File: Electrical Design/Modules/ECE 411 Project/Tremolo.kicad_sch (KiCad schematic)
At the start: 14 parts, among them Q1 NPN, U7 TL072

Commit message: kicad business
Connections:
- net In renamed TREMIN
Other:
- company: (none) -> Portland State University
- title: (none) -> Tremolo Effect
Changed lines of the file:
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@@
 	(generator_version "8.0")
 	(paper "A4")
+	(title_block
+		(title "Tremolo Effect")
+		(date "2024-10-31")
+		(rev "1.1")
+		(company "Portland State University")
+		(comment 1 "Open Source Hardware")
+		(comment 2 "Design: Eric Sanman, Sierra Buckley, Chuong Vo, Chris Crider")
+	)
 	(junction
 		(at 100.33 142.24)
@@
 		)
 	)
-	(hierarchical_label "In"
+	(hierarchical_label "TREMIN"
 		(shape input)
 		(at 99.06 80.01 90)
@@
 		)
 	)
-	(hierarchical_label "Out"
+	(hierarchical_label "TREMOUT"
 		(shape output)
 		(at 143.51 80.01 0)

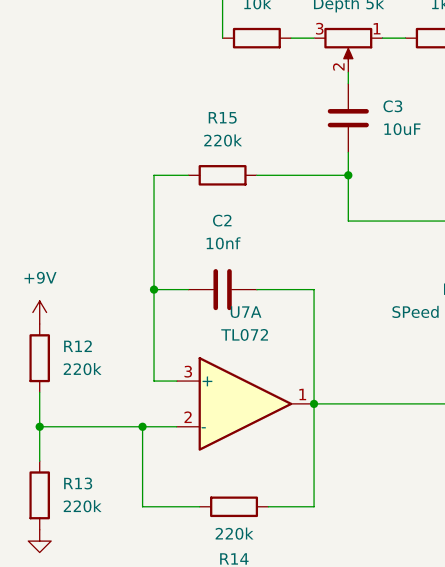
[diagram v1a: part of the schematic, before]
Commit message: add psu and fix schematic
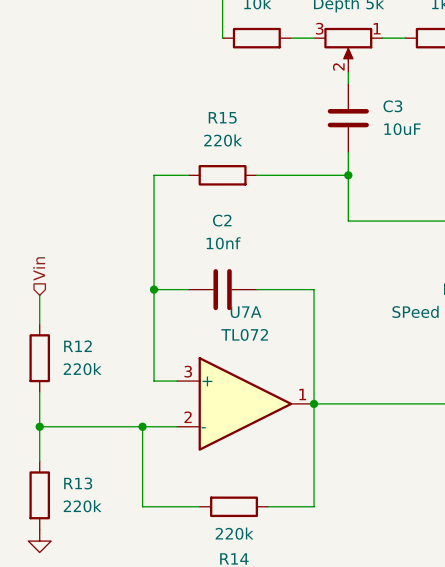
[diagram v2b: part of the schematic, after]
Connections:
- net +9V renamed Vin
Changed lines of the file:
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@@
+	(wire
+		(pts
+			(xy 87.63 142.875) (xy 87.63 146.05)
+		)
+		(stroke
+			(width 0)
+			(type default)
+		)
+	)
 	(wire
 		(pts
@@
 		)
 	)
+	(hierarchical_label "Vin"
+		(shape input)
+		(at 87.63 142.875 90)
+		(fields_autoplaced yes)
+		(effects
+			(font
+				(size 1.27 1.27)
+			)
+			(justify left)
+		)
+	)
 	(hierarchical_label "TREMOUT"
 		(shape output)
@@
 					(unit 1)
 				)
-			)
-		)
-	)
-	(symbol
-		(lib_id "power:+9V")
-		(at 87.63 146.05 0)
-		(unit 1)
-		(exclude_from_sim no)
-		(in_bom yes)
-		(on_board yes)
-		(dnp no)
-		(fields_autoplaced yes)
-		(property "Reference" "#PWR09"
-			(at 87.63 149.86 0)
-			(effects
-				(font
-					(size 1.27 1.27)
-				)
-				(hide yes)
-			)
-		)
-		(property "Value" "+9V"
-			(at 87.63 140.97 0)
-			(effects
-				(font
-					(size 1.27 1.27)
-				)
-			)
-		)
-		(property "Footprint" ""
-			(at 87.63 146.05 0)
-			(effects
-				(font
-					(size 1.27 1.27)
-				)
-				(hide yes)
-			)
-		)
-		(property "Datasheet" ""
-			(at 87.63 146.05 0)
-			(effects
-				(font
-					(size 1.27 1.27)
-				)
-				(hide yes)
-			)
-		)
-		(property "Description" "Power symbol creates a global label with name \"+9V\""
-			(at 87.63 146.05 0)
-			(effects
-				(font
-					(size 1.27 1.27)
-				)
-				(hide yes)
-			)
-		)
-		(pin "1"
-		)
-		(instances
-			(project ""
-				(path "/2625e5a1-d0c8-41ce-941d-75d035a5f1c5/29e94901-2eb6-4d5f-9450-5a88f29fead6"
-					(reference "#PWR09")
-					(unit 1)
-				)

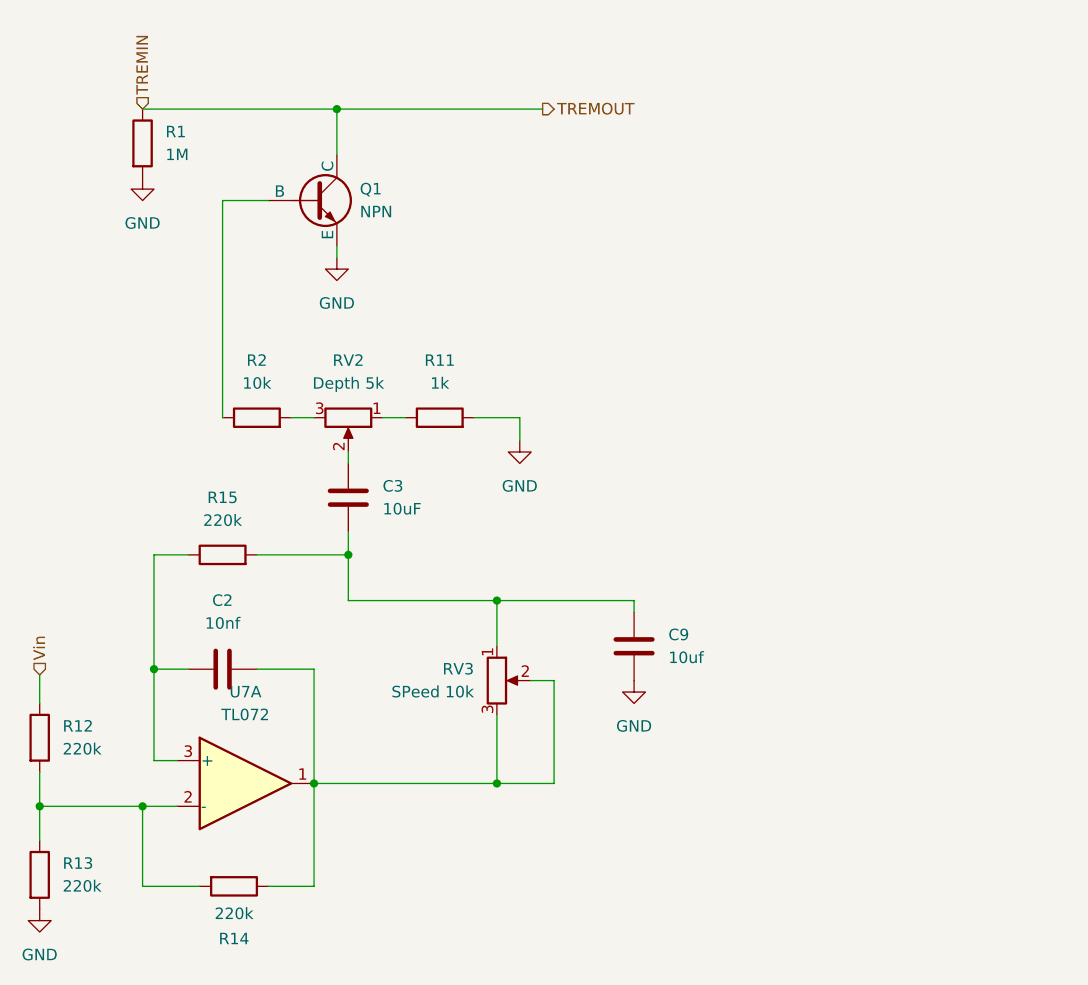
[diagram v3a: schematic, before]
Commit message: schematic, start layout
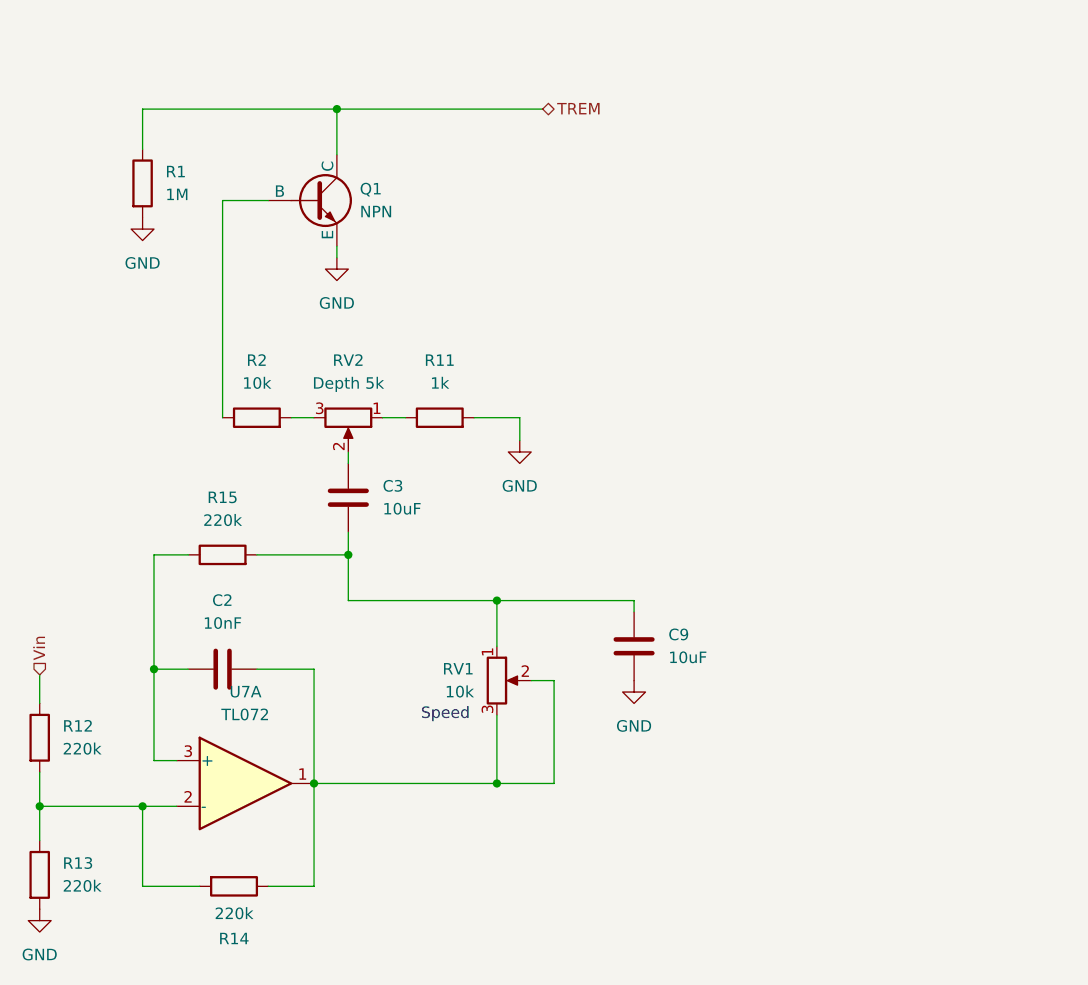
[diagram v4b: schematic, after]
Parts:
- C2: value 10nf -> 10nF; footprint (none) -> Capacitor_SMD:C_0805_2012Metric_Pad1.18x1.45mm_HandSolder
- C3: footprint (none) -> Capacitor_SMD:C_1210_3225Metric_Pad1.33x2.70mm_HandSolder
- C9: value 10uf -> 10uF; footprint (none) -> Capacitor_SMD:C_1206_3216Metric_Pad1.33x1.80mm_HandSolder
- Q1: footprint (none) -> Package_TO_SOT_THT:TO-52-3
- R1, R11, R12, R13, R14, R15, R2: footprint (none) -> Resistor_SMD:R_0805_2012Metric_Pad1.20x1.40mm_HandSolder
- RV1: renamed from RV3; value SPeed 10k -> 10k; footprint (none) -> Connector_PinHeader_2.54mm:PinHeader_1x03_P2.54mm_Vertical
- RV2: footprint (none) -> Connector_PinHeader_2.54mm:PinHeader_1x03_P2.54mm_Vertical
- U7: footprint (none) -> Package_DIP:CERDIP-8_W7.62mm_SideBrazed
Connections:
- net TREMIN renamed TREM
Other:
- note added: "Speed"
- moved on the sheet: R1
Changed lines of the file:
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@@
 	(title_block
 		(title "Tremolo Effect")
-		(date "2024-10-31")
-		(rev "1.1")
+		(date "2024-11-07")
+		(rev "1.5")
 		(company "Portland State University")
 		(comment 1 "Open Source Hardware")
@@
 	(wire
 		(pts
+			(xy 118.11 154.94) (xy 138.43 154.94)
+		)
+		(stroke
+			(width 0)
+			(type default)
+		)
+	)
+	(wire
+		(pts
 			(xy 121.92 119.38) (xy 121.92 118.11)
 		)
@@
 	(wire
 		(pts
+			(xy 99.06 80.01) (xy 99.06 84.455)
+		)
+		(stroke
+			(width 0)
+			(type default)
+		)
+	)
+	(wire
+		(pts
 			(xy 107.95 90.17) (xy 107.95 114.3)
 		)
@@
 		)
 	)
-	(wire
-		(pts
-			(xy 138.43 154.94) (xy 118.11 154.94)
-		)
-		(stroke
-			(width 0)
-			(type default)
-		)
-	)
-	(hierarchical_label "TREMIN"
-		(shape input)
-		(at 99.06 80.01 90)
-		(fields_autoplaced yes)
+	(text "Speed"
+		(exclude_from_sim no)
+		(at 132.715 147.32 0)
 		(effects
 			(font
 				(size 1.27 1.27)
 			)
-			(justify left)
 		)
 	)
@@
 		)
 	)
-	(hierarchical_label "TREMOUT"
-		(shape output)
+	(hierarchical_label "TREM"
+		(shape bidirectional)
 		(at 143.51 80.01 0)
 		(fields_autoplaced yes)
@@
 		(dnp no)
 		(fields_autoplaced yes)
-		(property "Reference" "RV3"
+		(property "Reference" "RV1"
 			(at 135.89 142.2399 0)
 			(effects
@@
 			)
 		)
-		(property "Value" "SPeed 10k"
+		(property "Value" "10k"
 			(at 135.89 144.7799 0)
 			(effects
@@
 			)
 		)
-		(property "Footprint" ""
+		(property "Footprint" "Connector_PinHeader_2.54mm:PinHeader_1x03_P2.54mm_Vertical"
 			(at 138.43 143.51 0)
 			(effects
@@
 			(project "ECE 411 Project"
 				(path "/2625e5a1-d0c8-41ce-941d-75d035a5f1c5/29e94901-2eb6-4d5f-9450-5a88f29fead6"
-					(reference "RV3")
+					(reference "RV1")
 					(unit 1)
 				)
@@
 			)
 		)
-		(property "Footprint" ""
+		(property "Footprint" "Package_TO_SOT_THT:TO-52-3"
 			(at 181.61 90.17 0)
 			(effects
@@
 			)
 		)
-		(property "Footprint" ""
+		(property "Footprint" "Capacitor_SMD:C_1210_3225Metric_Pad1.33x2.70mm_HandSolder"
 			(at 120.9548 119.38 0)
 			(effects
@@
 			)
 		)
-		(property "Footprint" ""
+		(property "Footprint" "Package_DIP:CERDIP-8_W7.62mm_SideBrazed"
 			(at 110.49 154.94 0)
 			(effects
@@
 			)
 		)
-		(property "Footprint" ""
+		(property "Footprint" "Resistor_SMD:R_0805_2012Metric_Pad1.20x1.40mm_HandSolder"
 			(at 107.95 131.318 90)
 			(effects
@@
 			)
 		)
-		(property "Value" "10uf"
+		(property "Value" "10uF"
 			(at 157.48 140.9699 0)
 			(effects
@@
 			)
 		)
-		(property "Footprint" ""
+		(property "Footprint" "Capacitor_SMD:C_1206_3216Metric_Pad1.33x1.80mm_HandSolder"
 			(at 152.7048 135.89 0)
 			(effects
@@
 			)
 		)
-		(property "Footprint" ""
+		(property "Footprint" "Resistor_SMD:R_0805_2012Metric_Pad1.20x1.40mm_HandSolder"
 			(at 109.22 164.592 90)
 			(effects
@@
 			)
 		)
-		(property "Footprint" ""
+		(property "Footprint" "Resistor_SMD:R_0805_2012Metric_Pad1.20x1.40mm_HandSolder"
 			(at 85.852 149.86 90)
 			(effects
@@
 	(symbol
 		(lib_id "power:GND")
-		(at 99.06 87.63 0)
+		(at 99.06 92.075 0)
 		(unit 1)
 		(exclude_from_sim no)
@@
 		(fields_autoplaced yes)
 		(property "Reference" "#PWR011"
-			(at 99.06 93.98 0)
+			(at 99.06 98.425 0)
 			(effects
 				(font
@@
 		)
 		(property "Value" "GND"
-			(at 99.06 92.71 0)
+			(at 99.06 97.155 0)
 			(effects
 				(font
@@
 		)
 		(property "Footprint" ""
-			(at 99.06 87.63 0)
+			(at 99.06 92.075 0)
 			(effects
 				(font
@@
 		)
 		(property "Datasheet" ""
-			(at 99.06 87.63 0)
+			(at 99.06 92.075 0)
 			(effects
 				(font
@@
 		)
 		(property "Description" "Power symbol creates a global label with name \"GND\" , ground"
-			(at 99.06 87.63 0)
+			(at 99.06 92.075 0)
 			(effects
 				(font
@@
 			)
 		)
-		(property "Footprint" ""
+		(property "Footprint" "Resistor_SMD:R_0805_2012Metric_Pad1.20x1.40mm_HandSolder"
 			(at 111.76 116.078 90)
 			(effects
@@
 	(symbol
 		(lib_id "Device:R")
-		(at 99.06 83.82 0)
+		(at 99.06 88.265 0)
 		(unit 1)
 		(exclude_from_sim no)
@@
 		(fields_autoplaced yes)
 		(property "Reference" "R1"
-			(at 101.6 82.5499 0)
+			(at 101.6 86.9949 0)
 			(effects
 				(font
@@
 		)
 		(property "Value" "1M"
-			(at 101.6 85.0899 0)
+			(at 101.6 89.5349 0)
 			(effects
 				(font
@@
 			)
 		)
-		(property "Footprint" ""
-			(at 97.282 83.82 90)
+		(property "Footprint" "Resistor_SMD:R_0805_2012Metric_Pad1.20x1.40mm_HandSolder"
+			(at 97.282 88.265 90)
 			(effects
 				(font
@@
 		)
 		(property "Datasheet" "~"
-			(at 99.06 83.82 0)
+			(at 99.06 88.265 0)
 			(effects
 				(font
@@
 		)
 		(property "Description" "Resistor"
-			(at 99.06 83.82 0)
+			(at 99.06 88.265 0)
 			(effects
 				(font
@@
 			)
 		)
-		(property "Value" "10nf"
+		(property "Value" "10nF"
 			(at 107.95 137.16 90)
 			(effects
@@
 			)
 		)
-		(property "Footprint" ""
+		(property "Footprint" "Capacitor_SMD:C_0805_2012Metric_Pad1.18x1.45mm_HandSolder"
 			(at 111.76 141.2748 0)
 			(effects
@@
 			)
 		)
-		(property "Footprint" ""
+		(property "Footprint" "Resistor_SMD:R_0805_2012Metric_Pad1.20x1.40mm_HandSolder"
 			(at 132.08 116.078 90)
 			(effects
@@
 			)
 		)
-		(property "Footprint" ""
+		(property "Footprint" "Connector_PinHeader_2.54mm:PinHeader_1x03_P2.54mm_Vertical"
 			(at 121.92 114.3 0)
 			(effects
@@
 			)
 		)
-		(property "Footprint" ""
+		(property "Footprint" "Resistor_SMD:R_0805_2012Metric_Pad1.20x1.40mm_HandSolder"
 			(at 85.852 165.1 90)
 			(effects

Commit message: update kicad
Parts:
- removed C3: 10uF, Capacitor_SMD:C_1210_3225Metric_Pad1.33x2.70mm_HandSolder, symbol Device:C
- removed C9: 10uF, Capacitor_SMD:C_1206_3216Metric_Pad1.33x1.80mm_HandSolder, symbol Device:C
- removed Q1: NPN, Package_TO_SOT_THT:TO-52-3, symbol Simulation_SPICE:NPN
- removed R11: 1k, Resistor_SMD:R_0805_2012Metric_Pad1.20x1.40mm_HandSolder, symbol Device:R
- removed R12, R13, R14, R15: 220k, Resistor_SMD:R_0805_2012Metric_Pad1.20x1.40mm_HandSolder, symbol Device:R
- removed RV1: 10k, Connector_PinHeader_2.54mm:PinHeader_1x03_P2.54mm_Vertical, symbol Device:R_Potentiometer
- removed RV2: Depth 5k, Connector_PinHeader_2.54mm:PinHeader_1x03_P2.54mm_Vertical, symbol Device:R_Potentiometer
- removed U7: TL072, Package_DIP:CERDIP-8_W7.62mm_SideBrazed, symbol Amplifier_Operational:TL072
- added D3: LED, LED_THT:LED_D5.0mm, symbol Device:LED
- added RV6: 100k, Connector_PinSocket_2.54mm:PinSocket_1x03_P2.54mm_Vertical, symbol Device:R_Potentiometer
- added U4: NE555D, Package_SO:SOIC-8_3.9x4.9mm_P1.27mm, symbol Timer:NE555D
- added U5: LTV-827, Package_DIP:DIP-8_W7.62mm, symbol Isolator:LTV-827
- C2: value 10nF -> 4.7uF; footprint Capacitor_SMD:C_0805_2012Metric_Pad1.18x1.45mm_HandSolder -> Capacitor_SMD:C_1206_3216Metric_Pad1.33x1.80mm_HandSolder
- R1: value 1M -> 1.2k
- R2: value 10k -> 1.2k
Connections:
- net TREM is gone; now on net Vin: R1.1
- net GND: now also C2.1, D3.1 (K), U4.1 (GND); no longer R1.2
- net Vin: now also U4.4 (R), U4.8 (VCC)
- net at C2.2: now also RV6.1, U4.2 (TR), U4.6 (THR)
- net CLK: now reaches R2.1
- net CLK: now also U4.3 (Q)
- net at R2.2: now also U5.1
- new net: R1.2, RV6.2, U4.7 (DIS)
- new net: D3.2 (A), U5.2
- new net TREMIN: U5.8
- new net TREMOUT: U5.7
- no-connect marks 0 -> 2
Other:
- note removed: "Speed"

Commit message: update BOM
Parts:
- C2: On Hand (On Way) (none) -> (100); Part Number (none) -> CL31B475KAHNNNE; Part Origin (none) -> DK
- D3, R1, R2, RV6, U4: Part Origin (none) -> DK
- U5: Part Origin (none) -> SBP
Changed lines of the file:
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@@
+			)
+		)
+		(property "Part Number" ""
+			(at 135.255 116.205 0)
+			(effects
+				(font
+					(size 1.27 1.27)
+				)
+				(hide yes)
+			)
+		)
+		(property "Part Origin" "DK"
+			(at 135.255 116.205 0)
+			(effects
+				(font
+					(size 1.27 1.27)
+				)
+				(hide yes)
+			)
+		)
+		(property "On Hand (On Way)" ""
+			(at 135.255 116.205 0)
+			(effects
+				(font
+					(size 1.27 1.27)
+				)
+				(hide yes)
 			)
 		)
@@
 			)
 		)
+		(property "Part Number" "CL31B475KAHNNNE"
+			(at 112.395 103.505 0)
+			(effects
+				(font
+					(size 1.27 1.27)
+				)
+				(hide yes)
+			)
+		)
+		(property "Part Origin" "DK"
+			(at 112.395 103.505 0)
+			(effects
+				(font
+					(size 1.27 1.27)
+				)
+				(hide yes)
+			)
+		)
+		(property "On Hand (On Way)" "(100)"
+			(at 112.395 103.505 0)
+			(effects
+				(font
+					(size 1.27 1.27)
+				)
+				(hide yes)
+			)
+		)
 		(pin "1"
 		)
@@
 			)
 		)
+		(property "Part Number" ""
+			(at 140.335 94.615 0)
+			(effects
+				(font
+					(size 1.27 1.27)
+				)
+				(hide yes)
+			)
+		)
+		(property "Part Origin" "DK"
+			(at 140.335 94.615 0)
+			(effects
+				(font
+					(size 1.27 1.27)
+				)
+				(hide yes)
+			)
+		)
+		(property "On Hand (On Way)" ""
+			(at 140.335 94.615 0)
+			(effects
+				(font
+					(size 1.27 1.27)
+				)
+				(hide yes)
+			)
+		)
 		(pin "1"
 		)
@@
 			)
 		)
+		(property "Part Number" ""
+			(at 149.86 89.535 0)
+			(effects
+				(font
+					(size 1.27 1.27)
+				)
+				(hide yes)
+			)
+		)
+		(property "Part Origin" "DK"
+			(at 149.86 89.535 0)
+			(effects
+				(font
+					(size 1.27 1.27)
+				)
+				(hide yes)
+			)
+		)
+		(property "On Hand (On Way)" ""
+			(at 149.86 89.535 0)
+			(effects
+				(font
+					(size 1.27 1.27)
+				)
+				(hide yes)
+			)
+		)
 		(pin "2"
 		)
@@
 			)
 		)
+		(property "Part Number" ""
+			(at 166.37 111.125 0)
+			(effects
+				(font
+					(size 1.27 1.27)
+				)
+				(hide yes)
+			)
+		)
+		(property "Part Origin" "DK"
+			(at 166.37 111.125 0)
+			(effects
+				(font
+					(size 1.27 1.27)
+				)
+				(hide yes)
+			)
+		)
+		(property "On Hand (On Way)" ""
+			(at 166.37 111.125 0)
+			(effects
+				(font
+					(size 1.27 1.27)
+				)
+				(hide yes)
+			)
+		)
 		(pin "2"
 		)
@@
 			)
 		)
+		(property "Part Number" ""
+			(at 158.75 124.46 0)
+			(effects
+				(font
+					(size 1.27 1.27)
+				)
+				(hide yes)
+			)
+		)
+		(property "Part Origin" "DK"
+			(at 158.75 124.46 0)
+			(effects
+				(font
+					(size 1.27 1.27)
+				)
+				(hide yes)
+			)
+		)
+		(property "On Hand (On Way)" ""
+			(at 158.75 124.46 0)
+			(effects
+				(font
+					(size 1.27 1.27)
+				)
+				(hide yes)
+			)
+		)
 		(pin "2"
 		)
@@
 			(at 180.34 113.665 0)
 			(effects
+				(font
+					(size 1.27 1.27)
+				)
+				(hide yes)
+			)
+		)
+		(property "Part Number" ""
+			(at 180.34 113.665 0)
+			(effects
+				(font
+					(size 1.27 1.27)
+				)
+				(hide yes)
+			)
+		)
+		(property "Part Origin" "SBP"
+			(at 180.34 113.665 0)
+			(effects
+				(font
+					(size 1.27 1.27)
+				)
+				(hide yes)
+			)
+		)
+		(property "On Hand (On Way)" ""
+			(at 180.34 113.665 0)
+			(effects
